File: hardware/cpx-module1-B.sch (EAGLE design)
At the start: 72 parts, among them IC1 CIRCUITPLAYGROUNDEXPRESS, IC2 MCP6004, IC3 TL074, IC4 LM4040DIM3-5.0, J1 WQP-PJ301M-12_JACK, J2 WQP-PJ301M-12_JACK, J3 WQP-PJ301M-12_JACK, J4 WQP-PJ301M-12_JACK, J5 WQP-PJ301M-12_JACK, J6 WQP-PJ301M-12_JACK, J7 WQP-PJ301M-12_JACK, J8 WQP-PJ301M-12_JACK

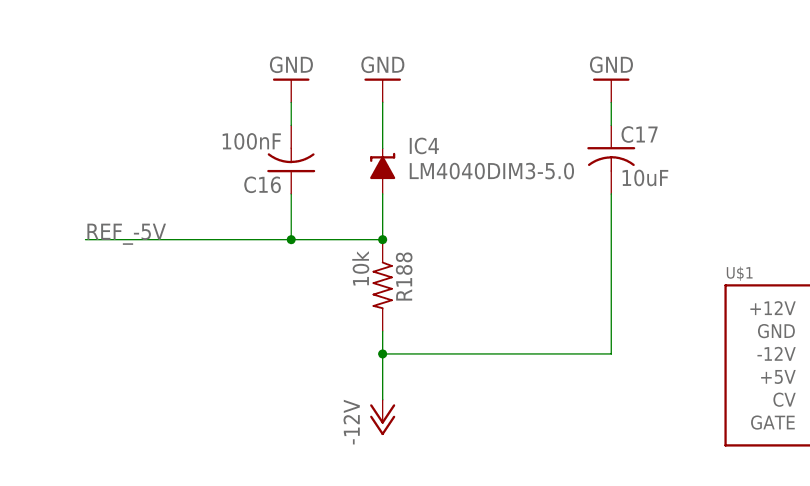
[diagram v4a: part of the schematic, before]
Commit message: fix silkscreen a little
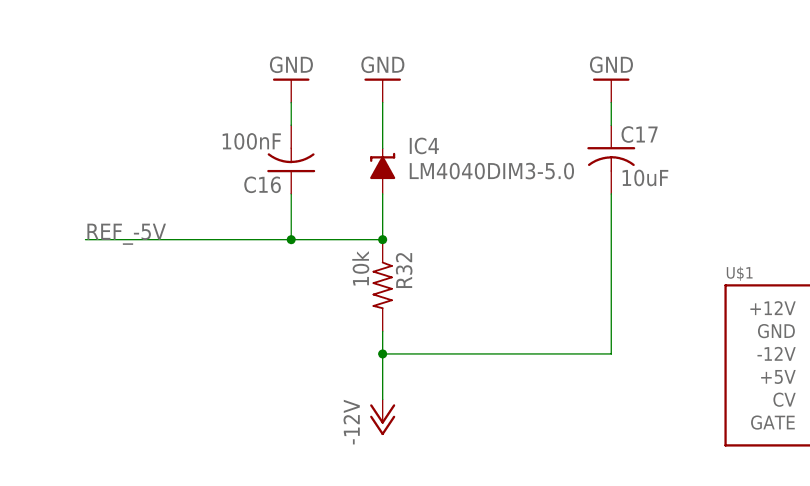
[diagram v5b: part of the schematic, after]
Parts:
- renumbered R188 to R32
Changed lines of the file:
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@@
 <part name="GND17" library="supply1" library_urn="urn:adsk.eagle:library:371" deviceset="GND" device=""/>
 <part name="IC4" library="texas" library_urn="urn:adsk.eagle:library:387" deviceset="LM4041" device="DBZ" technology="B12" value="LM4040DIM3-5.0"/>
-<part name="R188" library="adafruit" library_urn="urn:adsk.eagle:library:420" deviceset="R-US_" device="R0603" value="10k"/>
+<part name="R32" library="adafruit" library_urn="urn:adsk.eagle:library:420" deviceset="R-US_" device="R0603" value="10k"/>
 <part name="GND23" library="supply1" library_urn="urn:adsk.eagle:library:371" deviceset="GND" device=""/>
 <part name="C17" library="rcl" library_urn="urn:adsk.eagle:library:334" deviceset="C-US" device="C0603" package3d_urn="urn:adsk.eagle:package:23616/2" value="10uF"/>
@@
 <attribute name="VALUE" x="43.434" y="-51.689" size="1.778" layer="96"/>
 </instance>
-<instance part="R188" gate="G$1" x="40.64" y="-63.5" rot="R270"/>
+<instance part="R32" gate="G$1" x="40.64" y="-63.5" rot="R270"/>
 <instance part="GND23" gate="1" x="30.48" y="-40.64" rot="R180"/>
 <instance part="C17" gate="G$1" x="66.04" y="-48.26"/>
@@
 <segment>
 <pinref part="P-2" gate="1" pin="-12V"/>
-<pinref part="R188" gate="G$1" pin="2"/>
+<pinref part="R32" gate="G$1" pin="2"/>
 <wire x1="40.64" y1="-76.2" x2="40.64" y2="-71.12" width="0.1524" layer="91"/>
 <wire x1="40.64" y1="-71.12" x2="40.64" y2="-68.58" width="0.1524" layer="91"/>
@@
 <net name="REF_-5V" class="0">
 <segment>
-<pinref part="R188" gate="G$1" pin="1"/>
+<pinref part="R32" gate="G$1" pin="1"/>
 <pinref part="IC4" gate="G$1" pin="A"/>
 <wire x1="40.64" y1="-58.42" x2="40.64" y2="-53.34" width="0.1524" layer="91"/>
